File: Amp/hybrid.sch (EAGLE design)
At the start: 122 parts, among them IC1 TL071P, IC2 TL071P, IC3 LM317MABT-OUT, IC4 LM317MABT-OUT, J1 RCJ-21XXMILL, J2 NRJ3HF-1, J3 703W-00/54, Q1 BC560KINKED, Q10 BC560KINKED, Q11 BC560KINKED, Q12 BC560KINKED, Q13 BC556KINKED, Q14 BC550KINKED, Q15 BC550KINKED, Q16 BC560KINKED, Q17 BD140, Q18 BD139, Q19 KSP43, Q2 BC560KINKED, Q3 BC560KINKED, Q4 BC556KINKED, Q5 BC550KINKED, Q6 BC550KINKED, Q7 BC560KINKED, Q8 BD140, Q9 BD139, T1 TR-LP30-1600

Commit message: Small changes
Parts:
- removed C30: 1uF, SparkFun-Capacitors:CAPPTH
- removed C31, C32: 47uF, my-cap:CAP_POLPTH-8/3.5
- removed F1: (no value), fuse:SH22,5
- removed H5: MOUNT-HOLE3.2, holes:MOUNT-HOLE3.2
- removed J1: RCJ-21XXMILL, my:RCJ-21XXMILL
- removed J3: 703W-00/54, my-conn:703W-00/54
- removed S1: SW-M2012SA2W40, my-sw:SW-M2012SA2W40
- removed T1: TR-LP30-1600, my-transformers:TR-LP30-1600
- removed U$1: ACRIDA-LOGO, my-logo:ACRIDA-LOGO
- added C25: 10uF, my-cap:CAP_POLPTH-6.5/2.5
- added H1: MOUNT-PAD-ROUND3.2, holes:MOUNT-PAD-ROUND3.2
- added LOGO1: ACRIDA-LOGO, my-logo:ACRIDA-LOGO
- added Q20: BD139, transistor-npn:BD139
- added Q21, Q22: KSP43, my-tran:KSP43
- added R46: 23.7k, SparkFun-Resistors:RESISTORPTH-1/4W
- added R47: 3.3k, SparkFun-Resistors:RESISTORPTH-1/4W
- added R48: 220, SparkFun-Resistors:RESISTORPTH-1/4W
- added X1: (no value), con-wago-508:W237-3E
- added X2: (no value), con-wago-508:W237-2N
- C1, C11: value 0.1uF -> 1uF; device SparkFun-Capacitors:CAPPTH -> capacitor-wima:C5/5
- C10: value 470uF -> 1uF; device my-cap:CAP_POLPTH-12.5/5 -> capacitor-wima:C5/5
- C12, C2: value 0.1uF -> 1uF
- C13: value 1uF -> 0.33u; device capacitor-wima:C5/5 -> capacitor-wima:C5/7.2
- C14: value 0.33u -> 100uF; device capacitor-wima:C5/3.5 -> my-cap:CAP_POLPTH-8/3.5
- C15: value 10p -> 100uF; device SparkFun-Capacitors:CAPPTH -> my-cap:CAP_POLPTH-12.5/5
- C16, C6: device my-cap:CAP_POLPTH-8/3.5 -> my-cap:CAP_POLPTH-12.5/5
- C17, C18, C8: value 47uF -> 470uF; device my-cap:CAP_POLPTH-8/3.5 -> my-cap:CAP_POLPTH-12.5/5
- C19, C20: device my-cap:CAP_POLPTH-12.5/5 -> my-cap:CAP_POLPTH-18/7.5
- C21: value 470uF -> 4700uF; device my-cap:CAP_POLPTH-18/7.5 -> my-cap:CAP_POLSNAPIN-30/10
- C22: value 470uF -> 1uF; device my-cap:CAP_POLPTH-18/7.5 -> SparkFun-Capacitors:CAPPTH1
- C23: value 4700uF -> 47uF; device my-cap:CAP_POLSNAPIN-30/10 -> my-cap:CAP_POLPTH-12/5
- C24: value 1uF -> 10uF; device SparkFun-Capacitors:CAPPTH -> my-cap:CAP_POLPTH-5/2.5
- C26: value 47uF -> 1uF; device my-cap:CAP_POLPTH-12/5 -> SparkFun-Capacitors:CAPPTH
- C27: value 10uF -> 1uF; device my-cap:CAP_POLPTH-5/2.5 -> SparkFun-Capacitors:CAPPTH
- C28: value 10uF -> 100uF; device my-cap:CAP_POLPTH-6.5/2.5 -> my-cap:CAP_POLPTH-12.5/5
- C29: value 1uF -> 100uF; device SparkFun-Capacitors:CAPPTH -> my-cap:CAP_POLPTH-12.5/5
- C4: device capacitor-wima:C5/3.5 -> capacitor-wima:C5/7.2
- C5: value 10p -> 100uF; device SparkFun-Capacitors:CAPPTH -> my-cap:CAP_POLPTH-8/3.5
- C7: value 47uF -> 100uF; device my-cap:CAP_POLPTH-8/3.5 -> my-cap:CAP_POLPTH-12.5/5
- H4: value MOUNT-PAD-ROUND3.2 -> MOUNT-HOLE3.2; device holes:MOUNT-PAD-ROUND3.2 -> holes:MOUNT-HOLE3.2
- IC3, IC4: value LM317MABT-OUT -> LM317MABT; device my-reg:LM317MABT-OUT -> my-reg:LM317MABT
- Q1, Q11: value BC560KINKED -> KSP06KINKED; device my-tran:BC560KINKED -> my-tran:KSP06KINKED
- Q10: value BC560KINKED -> BD139; device my-tran:BC560KINKED -> transistor-npn:BD139
- Q13, Q4: value BC556KINKED -> BC560KINKED; device my-tran:BC556KINKED -> my-tran:BC560KINKED
- Q14: value BC550KINKED -> BC560KINKED; device my-tran:BC550KINKED -> my-tran:BC560KINKED
- Q15, Q5: value BC550KINKED -> BC556KINKED; device my-tran:BC550KINKED -> my-tran:BC556KINKED
- Q16, Q7: value BC560KINKED -> BC550KINKED; device my-tran:BC560KINKED -> my-tran:BC550KINKED
- Q17: value BD140 -> BC550KINKED; device transistor-pnp:BD140 -> my-tran:BC550KINKED
- Q18: value BD139 -> BC560KINKED; device transistor-npn:BD139 -> my-tran:BC560KINKED
- Q19: value KSP43 -> BD140; device my-tran:KSP43 -> transistor-pnp:BD140
- Q8: value BD140 -> BC560KINKED; device transistor-pnp:BD140 -> my-tran:BC560KINKED
- Q9: value BD139 -> BD140; device transistor-npn:BD139 -> transistor-pnp:BD140
- R1: value 100k -> 1Meg
- R10, R30: value 2.2k -> 4.7k
- R12, R31: value 10k -> 2.2k
- R13: value 4.7k -> 10k
- R14: value 10k -> 4.7k; device SparkFun-Electromechanical:TRIMPOT3362U-2 -> SparkFun-Resistors:RESISTORPTH-1/4W
- R15, R35: value 220 -> 10k; device SparkFun-Resistors:RESISTORPTH-1/4W -> SparkFun-Electromechanical:TRIMPOT3362U-2
- R17, R36, R37: value 2.2 -> 220
- R19, R38: value 2.2k -> 2.2
- R2: value 1Meg -> 2Meg
- R20: value 100k -> 2.2k
- R22, R3: value 100k -> 2Meg
- R23: value 330 -> 2Meg
- R24: value 27k -> 1Meg
- R25, R6: value 1Meg -> 330
- R27: value 820 -> 5.1k
- R28: value 4.7k -> 330
- R29: value 2.2k -> 820
- R32: value 4.7k -> 2.2k
- R33: device SparkFun-Electromechanical:TRIMPOT3362U-2 -> SparkFun-Resistors:RESISTORPTH-1/4W
- R34: value 220 -> 4.7k
- R39: value 0.51 -> 2.2; device my-res:RESISTORPTH-1/2W -> SparkFun-Resistors:RESISTORPTH-1/4W
- R4: value 330 -> 1Meg
- R41: value 240 -> 0.51; device SparkFun-Resistors:RESISTORPTH-1/4W -> my-res:RESISTORPTH-1/2W
- R42: value 5.49k -> 2.2k
- R43: value 510 -> 240
- R44: value 23.7k -> 5.49k
- R45: value 3.3k -> 510
- R5: value 27k -> 330
- R7: value 330 -> 5.1k
- R8: value 820 -> 330
- R9: value 4.7k -> 820
- V1: device my-tubes:6DJ8-P-HORIZONTAL -> my-tubes:6DJ8-P21MM-BASE
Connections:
- removed net N$40: F1.1, J3L.P$1
- removed net N$44: F1.2, S1.P
- removed net N$45: S1.O, T1.4
- new net N$47: Q1.E, R7.2
- new net N$48: Q11.E, R27.2
- net +6.3FIL: now also R41.2, V1".H1; no longer R39.2, V1HEATER.H1
- net +LV: now also C21.+; no longer C23.+
- net AC_1: now also X2-2.KL; no longer T1.8
- net AC_2: now also C19.-, X2-1.KL; no longer C21.-, T1.5
- net CAT_L: now also R10.2; no longer R8.2
- net CAT_R: now also R29.2, R30.2; no longer R27.2, R28.2
- net FB_L: now also C5.-, C8.+, R1.2, R18.1, R19.2; no longer C10.+, C6.-, R17.1, R18.2, R2.2
- net FB_R: now also C14.-, C17.+, C18.+, R38.1, R39.2; no longer C16.-, C19.+, C20.+, R36.1, R37.2
- net FGND: now also V1".H3; no longer V1HEATER.H2
- net GND: now also C10.1, C15.-, C16.-, C20.-, C21.-, C22.2, C24.-, C25.-, C26.2, C27.2, C29.-, C6.-, H1.MOUNT, Q10.E, Q20.E, R12.1, R17.1, R23.2, R24.1, R29.1, R3.2, R32.1, R37.1, R4.1, R40.1, R46.2, R7.1, R9.1, X1-2.KL; no longer C11.1, C17.-, C18.-, C22.-, C24.2, C26.-, C27.-, C29.2, C30.2, C31.-, C32.-, C8.-, H4.MOUNT, J1A.S, J1B.S, Q18.E, Q9.E, R1.1, R11.1, R16.1, R19.1, R25.1, R30.1, R35.1, R38.1, R42.2, R6.1, R8.1, V1GNDPLANE.GND
- net G_L: now also R4.2, R5.2; no longer R6.2, V1A.TG
- net G_R: now also C13.2, R24.2; no longer C14.2, V1B.TG
- net HT: now also C15.+, C29.+, C6.+, R11.2, R28.2, R31.2, R45.1, R6.2, R8.2; no longer C17.+, C32.+, C7.+, R10.2, R23.2, R29.2, R4.2, R43.1, R7.2
- net IN_L: now also VR1A.S; no longer VR1B.S
- net IN_L*: now also VR1A.E, X1-1.KL; no longer J1B.T, VR1B.E
- net IN_R: now also C13.1, VR1B.S; no longer C14.1, VR1A.S
- net IN_R*: now also VR1B.E, X1-3.KL; no longer J1A.T, VR1A.E
- net ISET_L: now also Q2.C, Q4.B; no longer Q3.B, R5.2
- net ISET_R: now also Q11.C, Q12.C, Q14.B; no longer Q10.C, Q12.B, R24.2
- net N$1: now also Q3.B, Q3.C, Q4.E; no longer Q1.B, Q2.C, Q3.E
- net N$10: now also R14.2, R15.CW; no longer R13.2, R14.CW
- net N$11: now also Q7.E, Q9.C, R18.2; no longer Q6.E, Q8.C, R17.2
- net N$12: now also Q6.E, Q8.B, R12.2, R15.CCW, R15.WIPER; no longer Q5.E, Q7.B, R11.2, R14.CCW, R14.WIPER
- net N$13: now also Q10.C, Q8.E, R19.1; no longer Q7.E, Q9.C, R18.1
- net N$14: now also Q7.C, Q9.B, R16.1; no longer Q6.C, Q8.B, R15.1
- net N$15: now also Q10.B, Q8.C, R17.2; no longer Q7.C, Q9.B, R16.2
- net N$16: now also Q13.E, R28.1; no longer Q11.E, R26.1
- net N$17: now also Q12.B, Q13.B, Q13.C, Q14.E; no longer Q10.B, Q11.B, Q11.C, Q12.E
- net N$18: now also Q21.B, Q22.E, R48.2; no longer J3N.P$1, T1.1
- net N$19: now also C14.+, R30.1; no longer C16.+, R28.1
- net N$2: now also Q3.E, R8.1; no longer Q2.E, R7.1
- net N$20: now also Q15.E, R31.1; no longer Q13.E, R29.1
- net N$21: now also Q15.C, Q16.C, Q17.B, R33.2; no longer C15.2, Q13.C, Q14.C, Q15.B, R31.2
- net N$22: now also Q16.B, R33.1, R34.1; no longer Q14.B, R31.1, R32.1
- net N$23: now also R34.2, R35.CW; no longer R32.2, R33.CW
- net N$24: now also Q16.E, Q18.B, R32.2, R35.CCW, R35.WIPER; no longer Q14.E, Q16.B, R30.2, R33.CCW, R33.WIPER
- net N$25: now also Q17.E, Q19.C, R38.2; no longer Q15.E, Q17.C, R36.2
- net N$26: now also Q18.E, Q20.C, R39.1; no longer Q16.E, Q18.C, R37.1
- net N$27: now also Q17.C, Q19.B, R36.1; no longer Q15.C, Q17.B, R34.1
- net N$28: now also Q18.C, Q20.B, R37.2; no longer Q16.C, Q18.B, R35.2
- net N$29: now also Q1.B; no longer R5.1
- net N$3: now also Q2.E, R6.1; no longer Q1.E, R4.1
- net N$30: now also C24.+, C26.1, R43.2, R44.1; no longer C27.+, C29.1, R41.2, R42.1
- net N$31: now also C19.+; no longer C21.+
- net N$32: now also R41.1; no longer R39.1
- net N$33: now also C20.+, Q21.C, Q22.C, R42.1; no longer C22.+, Q19.C, R40.1
- net N$34: now also C22.1, C23.+, Q22.B, R42.2; no longer C24.1, C26.+, Q19.B, R40.2
- net N$35: now also R3.1
- net N$36: now also C25.+, C27.1, R45.2, R46.1; no longer C28.+, C30.1, R43.2, R44.1
- net N$37: now also Q21.E, R48.1; no longer Q19.E
- net N$38: now also R1.1; no longer R1.2, R3.1
- net N$39: now also Q12.E, R26.1; no longer Q10.E, R23.1
- net N$4: now also C5.+, R10.1; no longer C6.+, R9.1
- net N$41: now also C11.2, IC2.-IN, R22.1, R23.1; no longer C13.1, IC2.OUT, R24.1
- net N$42: now also C10.2, IC2.+IN; no longer C13.2, IC2.-IN
- net N$43: now also C11.1, IC2.OUT, Q11.B; no longer C11.2, IC2.+IN, R20.2, R22.1
- net N$46: now also R47.2; no longer R45.2
- net N$5: now also Q5.E, R11.1; no longer Q4.E, R10.1
- net N$6: now also R5.1, V1A.TG; no longer T1.2, T1.3
- net N$7: now also Q6.C, Q7.B, R13.2; no longer C5.2, Q4.C, Q6.B, R12.2
- net N$8: now also Q6.B, R14.1; no longer Q5.B, R12.1
- net N$9: now also R25.1, V1B.TG; no longer T1.6, T1.7
- net OUT_L: now also C8.-, R20.2; no longer C10.-, R19.2
- net OUT_R: now also C17.-, C18.-, R40.2; no longer C19.-, C20.-, R38.2
- net PL_L: now also Q4.C, Q5.B; no longer C5.1, Q3.C, Q4.B
- net PL_R: now also Q14.C, Q15.B; no longer C15.1, Q12.C, Q13.B
- net VCC: now also C16.+, C28.+, C7.+, Q19.E, Q9.E, R16.2, R2.2, R36.2, R43.1, R47.1; no longer C18.+, C31.+, C8.+, Q17.E, Q8.E, R15.2, R3.2, R34.2, R41.1, R45.1

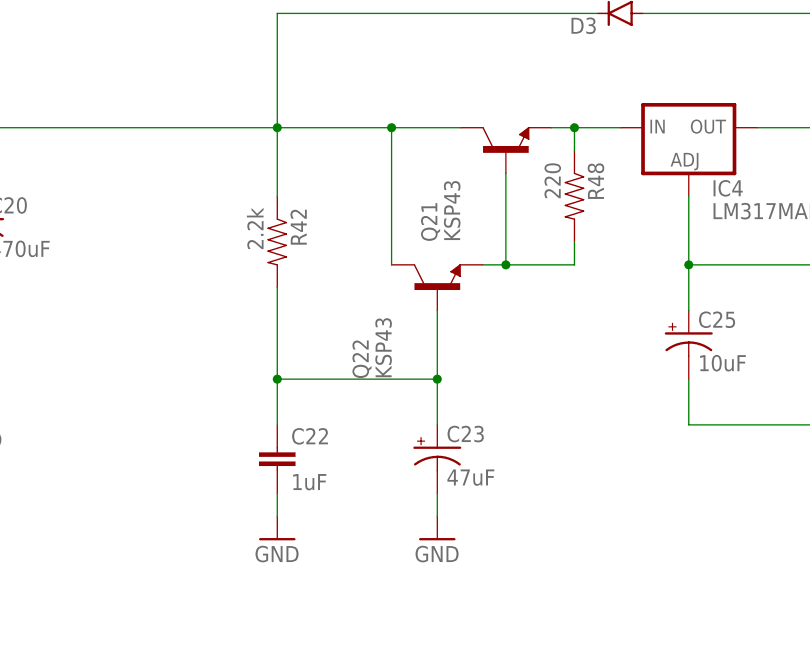
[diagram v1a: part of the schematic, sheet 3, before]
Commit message: Ground plane on top
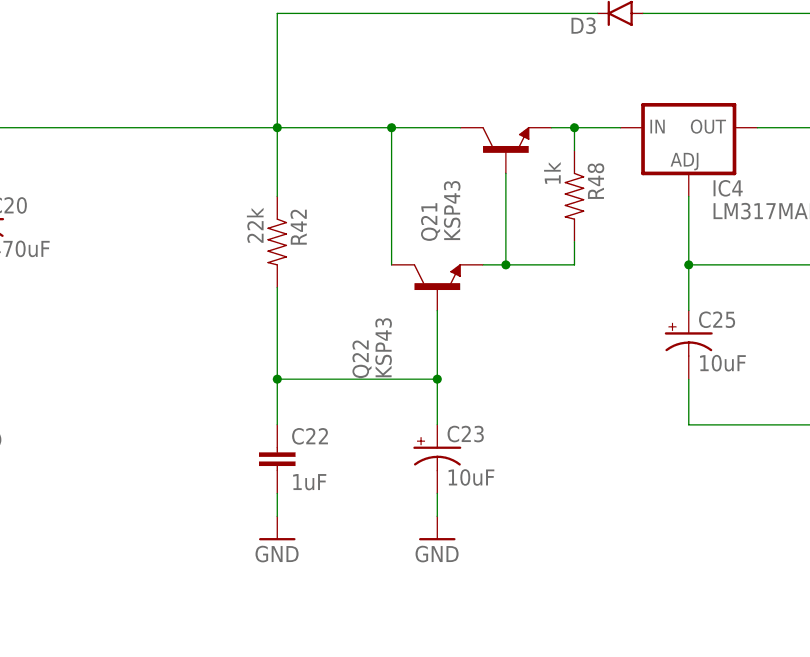
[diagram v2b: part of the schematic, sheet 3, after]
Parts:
- C23: value 47uF -> 10uF
- R42: value 2.2k -> 22k
- R48: value 220 -> 1k
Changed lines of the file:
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@@
 <grid distance="0.1" unitdist="inch" unit="inch" style="lines" multiple="1" display="no" altdistance="0.01" altunitdist="inch" altunit="inch"/>
 <layers>
-<layer number="1" name="Top" color="4" fill="1" visible="no" active="no"/>
-<layer number="2" name="Route2" color="1" fill="3" visible="no" active="no"/>
-<layer number="3" name="Route3" color="4" fill="3" visible="no" active="no"/>
-<layer number="4" name="Route4" color="1" fill="4" visible="no" active="no"/>
-<layer number="5" name="Route5" color="4" fill="4" visible="no" active="no"/>
-<layer number="6" name="Route6" color="1" fill="8" visible="no" active="no"/>
-<layer number="7" name="Route7" color="4" fill="8" visible="no" active="no"/>
-<layer number="8" name="Route8" color="1" fill="2" visible="no" active="no"/>
-<layer number="9" name="Route9" color="4" fill="2" visible="no" active="no"/>
-<layer number="10" name="Route10" color="1" fill="7" visible="no" active="no"/>
-<layer number="11" name="Route11" color="4" fill="7" visible="no" active="no"/>
-<layer number="12" name="Route12" color="1" fill="5" visible="no" active="no"/>
-<layer number="13" name="Route13" color="4" fill="5" visible="no" active="no"/>
-<layer number="14" name="Route14" color="1" fill="6" visible="no" active="no"/>
-<layer number="15" name="Route15" color="4" fill="6" visible="no" active="no"/>
-<layer number="16" name="Bottom" color="1" fill="1" visible="no" active="no"/>
-<layer number="17" name="Pads" color="2" fill="1" visible="no" active="no"/>
-<layer number="18" name="Vias" color="2" fill="1" visible="no" active="no"/>
-<layer number="19" name="Unrouted" color="6" fill="1" visible="no" active="no"/>
-<layer number="20" name="Dimension" color="15" fill="1" visible="no" active="no"/>
-<layer number="21" name="tPlace" color="7" fill="1" visible="no" active="no"/>
-<layer number="22" name="bPlace" color="7" fill="1" visible="no" active="no"/>
-<layer number="23" name="tOrigins" color="15" fill="1" visible="no" active="no"/>
-<layer number="24" name="bOrigins" color="15" fill="1" visible="no" active="no"/>
-<layer number="25" name="tNames" color="7" fill="1" visible="no" active="no"/>
-<layer number="26" name="bNames" color="7" fill="1" visible="no" active="no"/>
-<layer number="27" name="tValues" color="7" fill="1" visible="no" active="no"/>
-<layer number="28" name="bValues" color="7" fill="1" visible="no" active="no"/>
+<layer number="1" name="Top" color="4" fill="1" visible="yes" active="no"/>
+<layer number="2" name="Route2" color="1" fill="3" visible="yes" active="no"/>
+<layer number="3" name="Route3" color="4" fill="3" visible="yes" active="no"/>
+<layer number="4" name="Route4" color="1" fill="4" visible="yes" active="no"/>
+<layer number="5" name="Route5" color="4" fill="4" visible="yes" active="no"/>
+<layer number="6" name="Route6" color="1" fill="8" visible="yes" active="no"/>
+<layer number="7" name="Route7" color="4" fill="8" visible="yes" active="no"/>
+<layer number="8" name="Route8" color="1" fill="2" visible="yes" active="no"/>
+<layer number="9" name="Route9" color="4" fill="2" visible="yes" active="no"/>
+<layer number="10" name="Route10" color="1" fill="7" visible="yes" active="no"/>
+<layer number="11" name="Route11" color="4" fill="7" visible="yes" active="no"/>
+<layer number="12" name="Route12" color="1" fill="5" visible="yes" active="no"/>
+<layer number="13" name="Route13" color="4" fill="5" visible="yes" active="no"/>
+<layer number="14" name="Route14" color="1" fill="6" visible="yes" active="no"/>
+<layer number="15" name="Route15" color="4" fill="6" visible="yes" active="no"/>
+<layer number="16" name="Bottom" color="1" fill="1" visible="yes" active="no"/>
+<layer number="17" name="Pads" color="2" fill="1" visible="yes" active="no"/>
+<layer number="18" name="Vias" color="2" fill="1" visible="yes" active="no"/>
+<layer number="19" name="Unrouted" color="6" fill="1" visible="yes" active="no"/>
+<layer number="20" name="Dimension" color="15" fill="1" visible="yes" active="no"/>
+<layer number="21" name="tPlace" color="7" fill="1" visible="yes" active="no"/>
+<layer number="22" name="bPlace" color="7" fill="1" visible="yes" active="no"/>
+<layer number="23" name="tOrigins" color="15" fill="1" visible="yes" active="no"/>
+<layer number="24" name="bOrigins" color="15" fill="1" visible="yes" active="no"/>
+<layer number="25" name="tNames" color="7" fill="1" visible="yes" active="no"/>
+<layer number="26" name="bNames" color="7" fill="1" visible="yes" active="no"/>
+<layer number="27" name="tValues" color="7" fill="1" visible="yes" active="no"/>
+<layer number="28" name="bValues" color="7" fill="1" visible="yes" active="no"/>
 <layer number="29" name="tStop" color="7" fill="3" visible="no" active="no"/>
 <layer number="30" name="bStop" color="7" fill="6" visible="no" active="no"/>
@@
 <layer number="35" name="tGlue" color="7" fill="4" visible="no" active="no"/>
 <layer number="36" name="bGlue" color="7" fill="5" visible="no" active="no"/>
-<layer number="37" name="tTest" color="7" fill="1" visible="no" active="no"/>
-<layer number="38" name="bTest" color="7" fill="1" visible="no" active="no"/>
+<layer number="37" name="tTest" color="7" fill="1" visible="yes" active="no"/>
+<layer number="38" name="bTest" color="7" fill="1" visible="yes" active="no"/>
 <layer number="39" name="tKeepout" color="4" fill="11" visible="no" active="no"/>
 <layer number="40" name="bKeepout" color="1" fill="11" visible="no" active="no"/>
@@
 <layer number="44" name="Drills" color="7" fill="1" visible="no" active="no"/>
 <layer number="45" name="Holes" color="7" fill="1" visible="no" active="no"/>
-<layer number="46" name="Milling" color="3" fill="1" visible="no" active="no"/>
-<layer number="47" name="Measures" color="7" fill="1" visible="no" active="no"/>
-<layer number="48" name="Document" color="7" fill="1" visible="no" active="no"/>
-<layer number="49" name="Reference" color="7" fill="1" visible="no" active="no"/>
-<layer number="50" name="dxf" color="7" fill="1" visible="no" active="no"/>
-<layer number="51" name="tDocu" color="7" fill="1" visible="no" active="no"/>
-<layer number="52" name="bDocu" color="7" fill="1" visible="no" active="no"/>
-<layer number="53" name="tGND_GNDA" color="7" fill="9" visible="no" active="no"/>
-<layer number="54" name="bGND_GNDA" color="1" fill="9" visible="no" active="no"/>
-<layer number="56" name="wert" color="7" fill="1" visible="no" active="no"/>
-<layer number="57" name="tCAD" color="7" fill="1" visible="no" active="no"/>
-<layer number="59" name="tCarbon" color="7" fill="1" visible="no" active="no"/>
-<layer number="60" name="bCarbon" color="7" fill="1" visible="no" active="no"/>
+<layer number="46" name="Milling" color="3" fill="1" visible="yes" active="no"/>
+<layer number="47" name="Measures" color="7" fill="1" visible="yes" active="no"/>
+<layer number="48" name="Document" color="7" fill="1" visible="yes" active="no"/>
+<layer number="49" name="Reference" color="7" fill="1" visible="yes" active="no"/>
+<layer number="50" name="dxf" color="7" fill="1" visible="yes" active="no"/>
+<layer number="51" name="tDocu" color="7" fill="1" visible="yes" active="no"/>
+<layer number="52" name="bDocu" color="7" fill="1" visible="yes" active="no"/>
+<layer number="53" name="tGND_GNDA" color="7" fill="9" visible="yes" active="no"/>
+<layer number="54" name="bGND_GNDA" color="1" fill="9" visible="yes" active="no"/>
+<layer number="56" name="wert" color="7" fill="1" visible="yes" active="no"/>
+<layer number="57" name="tCAD" color="7" fill="1" visible="yes" active="no"/>
+<layer number="59" name="tCarbon" color="7" fill="1" visible="yes" active="no"/>
+<layer number="60" name="bCarbon" color="7" fill="1" visible="yes" active="no"/>
 <layer number="90" name="Modules" color="5" fill="1" visible="yes" active="yes"/>
 <layer number="91" name="Nets" color="2" fill="1" visible="yes" active="yes"/>
@@
 <part name="D3" library="SparkFun-DiscreteSemi" deviceset="DIODE" device="PTH"/>
 <part name="C29" library="my-cap" deviceset="CAP_POL" device="PTH-12.5/5" value="100uF"/>
-<part name="C23" library="my-cap" deviceset="CAP_POL" device="PTH-12/5" value="47uF"/>
+<part name="C23" library="my-cap" deviceset="CAP_POL" device="PTH-12/5" value="10uF"/>
 <part name="Q21" library="my-tran" deviceset="KSP43" device=""/>
 <part name="GND37" library="SparkFun-Aesthetics" deviceset="GND" device=""/>
-<part name="R42" library="SparkFun-Resistors" deviceset="RESISTOR" device="PTH-1/4W" value="2.2k"/>
+<part name="R42" library="SparkFun-Resistors" deviceset="RESISTOR" device="PTH-1/4W" value="22k"/>
 <part name="C22" library="SparkFun-Capacitors" deviceset="CAP" device="PTH1" value="1uF"/>
 <part name="GND36" library="SparkFun-Aesthetics" deviceset="GND" device=""/>
@@
 <part name="X2" library="con-wago-508" deviceset="W237-2N" device=""/>
 <part name="Q22" library="my-tran" deviceset="KSP43" device=""/>
-<part name="R48" library="SparkFun-Resistors" deviceset="RESISTOR" device="PTH-1/4W" value="220"/>
+<part name="R48" library="SparkFun-Resistors" deviceset="RESISTOR" device="PTH-1/4W" value="1k"/>
 </parts>
 <sheets>
